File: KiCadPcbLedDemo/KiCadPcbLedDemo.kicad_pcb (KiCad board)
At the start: 2 copper layers, 68.6 x 53.3 mm, 16 parts, among them P1 Power, P2 Analog, P3 Digital, P4 Digital, P5 CONN_01X01, P6 CONN_01X01, P7 CONN_01X01, P8 CONN_01X01

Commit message: Definir les contraintes de conception de la carte electronique
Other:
- net class Default: clearance 0.2 -> 0.8; trace_width 0.25 -> 0.8; via_dia 0.6 -> 1.2; via_drill 0.4 -> 0.8
- net class Power added: clearance 0.8, trace_width 1.2, via_dia 1.2, via_drill 0.8
- rule trace_clearance: 0.2 -> 0.8
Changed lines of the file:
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@@
     (0 F.Cu signal)
     (31 B.Cu signal)
-    (32 B.Adhes user)
     (33 F.Adhes user)
-    (34 B.Paste user)
     (35 F.Paste user)
-    (36 B.SilkS user)
     (37 F.SilkS user)
     (38 B.Mask user)
@@
     (46 B.CrtYd user)
     (47 F.CrtYd user hide)
-    (48 B.Fab user)
     (49 F.Fab user)
   )
   (setup
-    (last_trace_width 0.25)
-    (trace_clearance 0.2)
+    (last_trace_width 0.8)
+    (trace_clearance 0.8)
     (zone_clearance 0.508)
     (zone_45_only no)
     (trace_min 0.2)
-    (via_size 0.6)
-    (via_drill 0.4)
+    (via_size 1.2)
+    (via_drill 0.8)
     (via_min_size 0.4)
     (via_min_drill 0.3)
@@
   (net 36 /LED4)
   (net_class Default "This is the default net class."
-    (clearance 0.2)
-    (trace_width 0.25)
-    (via_dia 0.6)
-    (via_drill 0.4)
+    (clearance 0.8)
+    (trace_width 0.8)
+    (via_dia 1.2)
+    (via_drill 0.8)
     (uvia_dia 0.3)
     (uvia_drill 0.1)
     (add_net +3V3)
-    (add_net +5V)
     (add_net "/0(Rx)")
     (add_net "/1(Tx)")
@@
     (add_net "Net-(P8-Pad1)")
   )
+  (net_class Power ""
+    (clearance 0.8)
+    (trace_width 1.2)
+    (via_dia 1.2)
+    (via_drill 0.8)
+    (uvia_dia 0.3)
+    (uvia_drill 0.1)
+    (add_net +5V)
+  )
   (module Socket_Arduino_Uno:Socket_Strip_Arduino_1x08 locked (layer F.Cu)

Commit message: Add 3D view
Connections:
- P3 pad 1: /A5(SCL) -> Net-(P3-Pad1)
- P3 pad 2: /A4(SDA) -> Net-(P3-Pad2)
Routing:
- net /LED4: track 0.00 -> 46.6 mm
- net /LED3: track 0.00 -> 31.8 mm
- net /LED2: track 0.00 -> 24.1 mm
- net /LED1: track 0.00 -> 16.4 mm
- net Net-(D4-Pad2): track 0.00 -> 4.30 mm
- net Net-(D3-Pad2): track 0.00 -> 4.30 mm
- net Net-(D2-Pad2): track 0.00 -> 4.30 mm
- net Net-(D1-Pad2): track 0.00 -> 4.30 mm
- net GND: vias 0 -> 47
- added copper zone on B.Cu, net GND
- added copper zone on F.Cu, net GND

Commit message: Creation du symbole du capteur de gaz
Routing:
- net GND: vias 47 -> 37

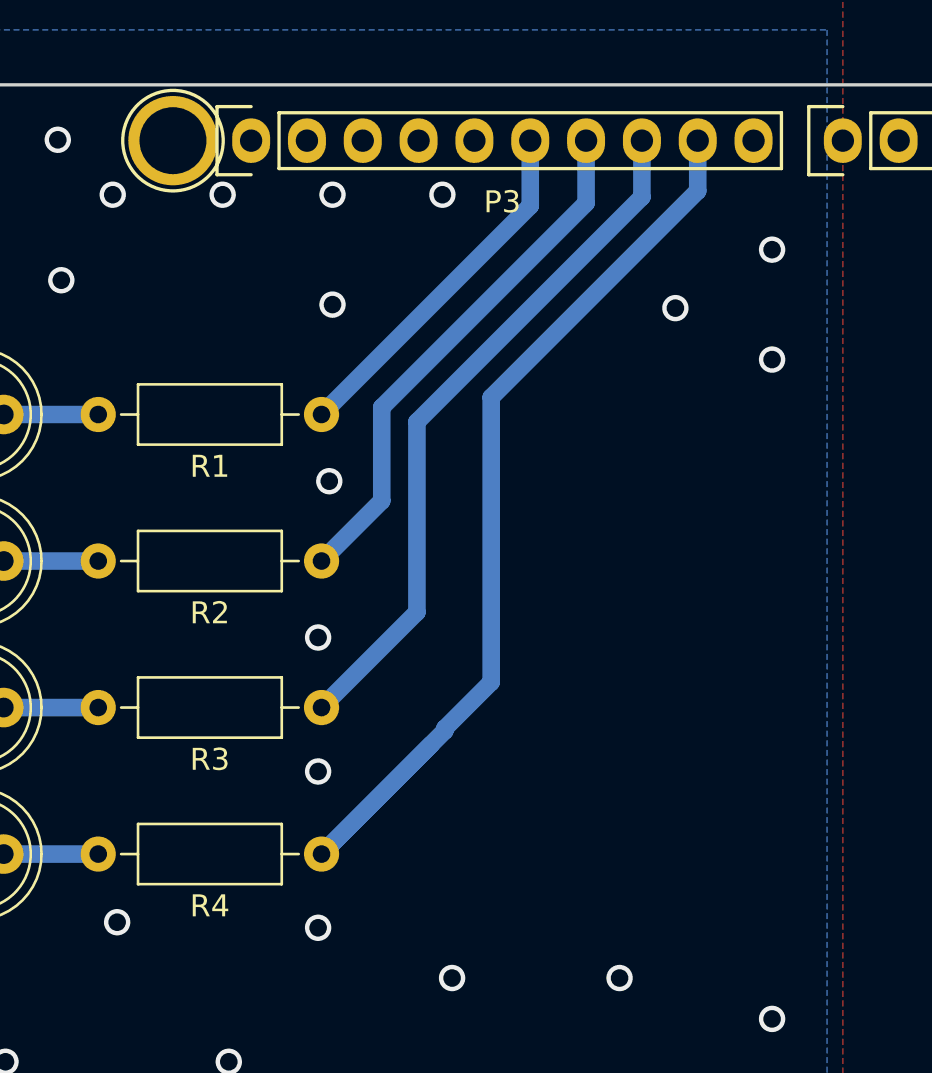
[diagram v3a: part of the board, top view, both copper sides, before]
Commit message: Routage de la carte avec le capteur de gaz
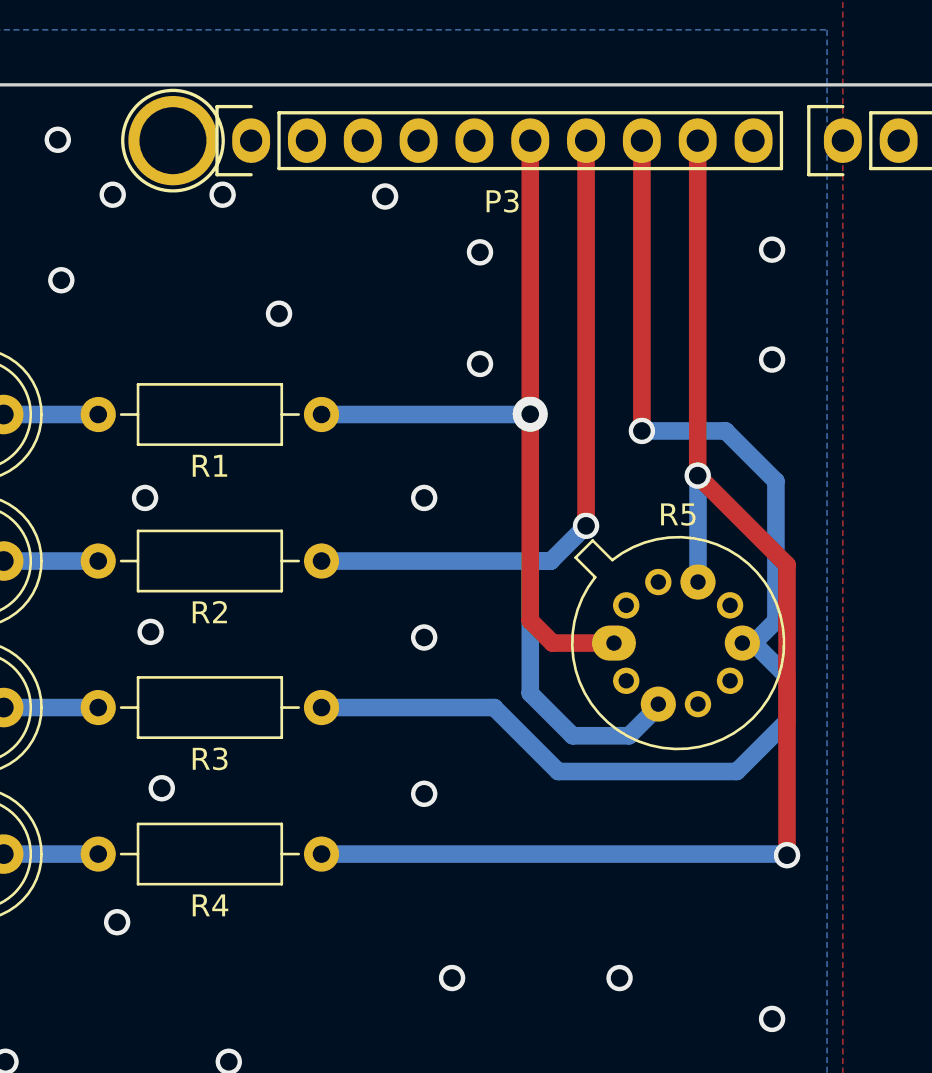
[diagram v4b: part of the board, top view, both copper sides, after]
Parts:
- added R5: GSensor, MyPackage:TO-5-10_Window, F.Cu at (146.3, 98.4)
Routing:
- net /LED3: track 31.8 -> 56.1 mm, vias 0 -> 1
- net /LED2: track 24.1 -> 45.1 mm, vias 0 -> 1
- net /LED1: track 16.4 -> 35.6 mm, vias 0 -> 1
- net /LED4: track 46.6 -> 60.2 mm, vias 0 -> 2
- net GND: vias 37 -> 39
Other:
- net class Power: via_dia 1.2 -> 1.6
